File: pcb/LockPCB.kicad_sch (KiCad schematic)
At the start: 0 parts

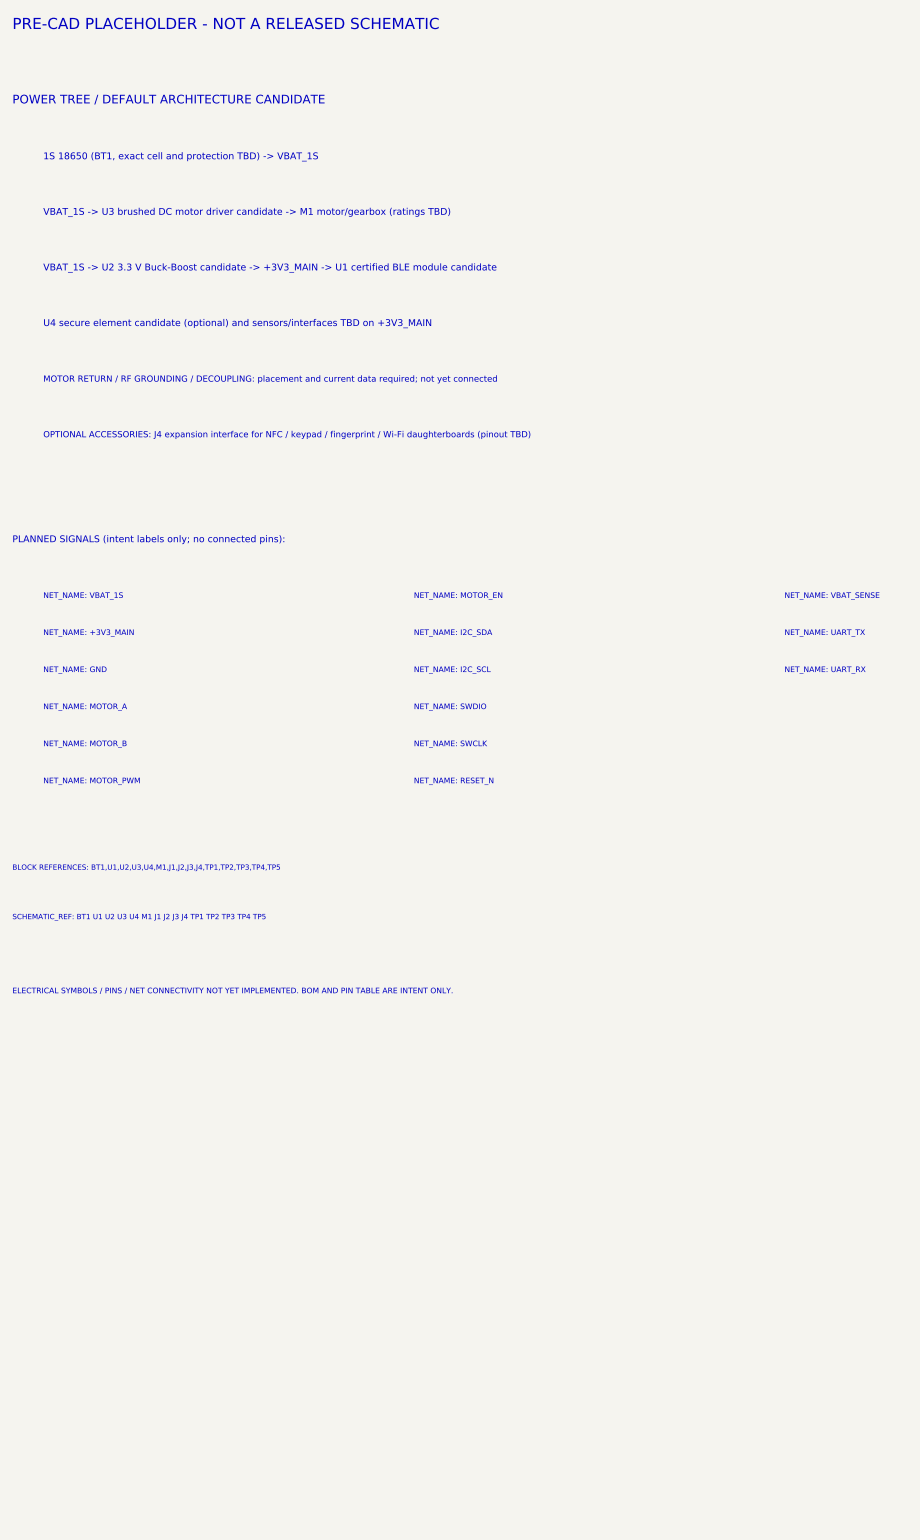
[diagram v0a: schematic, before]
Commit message: Record recommended blocker defaults and review envelope
Co-authored-by: arena-agent <297053741+arena-agent@users.noreply.github.com>
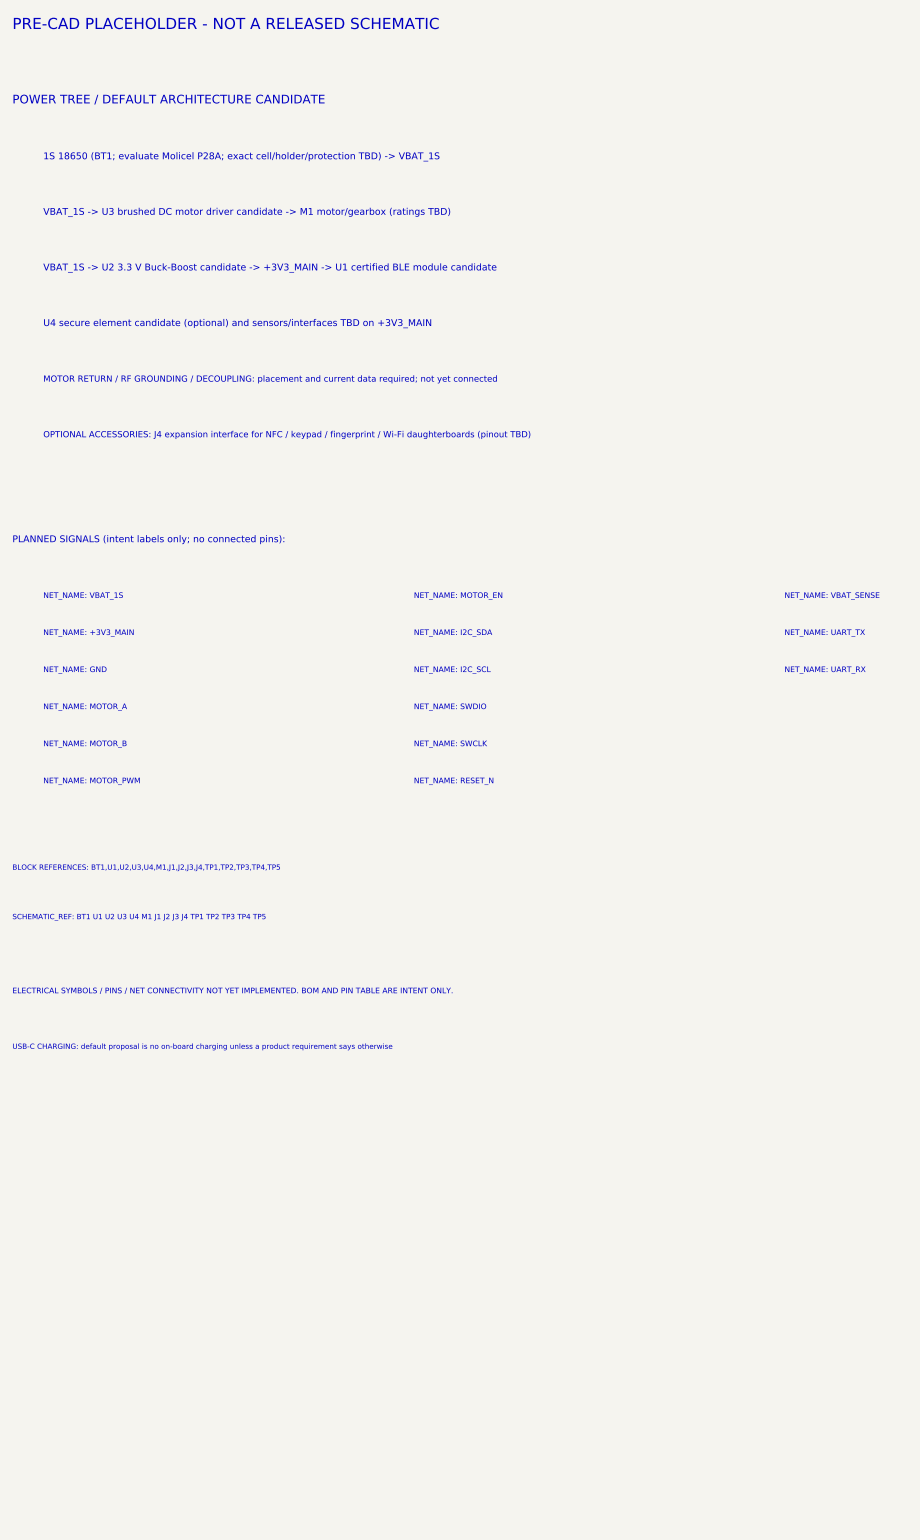
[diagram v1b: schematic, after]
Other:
- note added: "1S 18650 (BT1; evaluate Molicel P28A; exact cell/holder/protection TBD) -> VBAT_1S"
- note added: "USB-C CHARGING: default proposal is no on-board charging unless a product requirement says otherwise"
- note removed: "1S 18650 (BT1, exact cell and protection TBD) -> VBAT_1S"
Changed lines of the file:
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@@
   (text "PRE-CAD PLACEHOLDER - NOT A RELEASED SCHEMATIC" (at 25 28 0) (effects (font (size 1.8 1.8)) (justify left bottom)))
   (text "POWER TREE / DEFAULT ARCHITECTURE CANDIDATE" (at 25 40 0) (effects (font (size 1.4 1.4)) (justify left bottom)))
-  (text "1S 18650 (BT1, exact cell and protection TBD) -> VBAT_1S" (at 30 49 0) (effects (font (size 1.1 1.1)) (justify left bottom)))
+  (text "1S 18650 (BT1; evaluate Molicel P28A; exact cell/holder/protection TBD) -> VBAT_1S" (at 30 49 0) (effects (font (size 1.1 1.1)) (justify left bottom)))
   (text "VBAT_1S -> U3 brushed DC motor driver candidate -> M1 motor/gearbox (ratings TBD)" (at 30 58 0) (effects (font (size 1.1 1.1)) (justify left bottom)))
   (text "VBAT_1S -> U2 3.3 V Buck-Boost candidate -> +3V3_MAIN -> U1 certified BLE module candidate" (at 30 67 0) (effects (font (size 1.1 1.1)) (justify left bottom)))
@@
   (text "SCHEMATIC_REF: BT1 U1 U2 U3 U4 M1 J1 J2 J3 J4 TP1 TP2 TP3 TP4 TP5" (at 25 172 0) (effects (font (size 0.85 0.85)) (justify left bottom)))
   (text "ELECTRICAL SYMBOLS / PINS / NET CONNECTIVITY NOT YET IMPLEMENTED. BOM AND PIN TABLE ARE INTENT ONLY." (at 25 184 0) (effects (font (size 0.9 0.9)) (justify left bottom)))
+  (text "USB-C CHARGING: default proposal is no on-board charging unless a product requirement says otherwise" (at 25 193 0) (effects (font (size 0.85 0.85)) (justify left bottom)))
   (sheet_instances (path "/" (page "1")))
 )

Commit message: Reconcile Drive CAD history and expand interface intent
Co-authored-by: arena-agent <297053741+arena-agent@users.noreply.github.com>
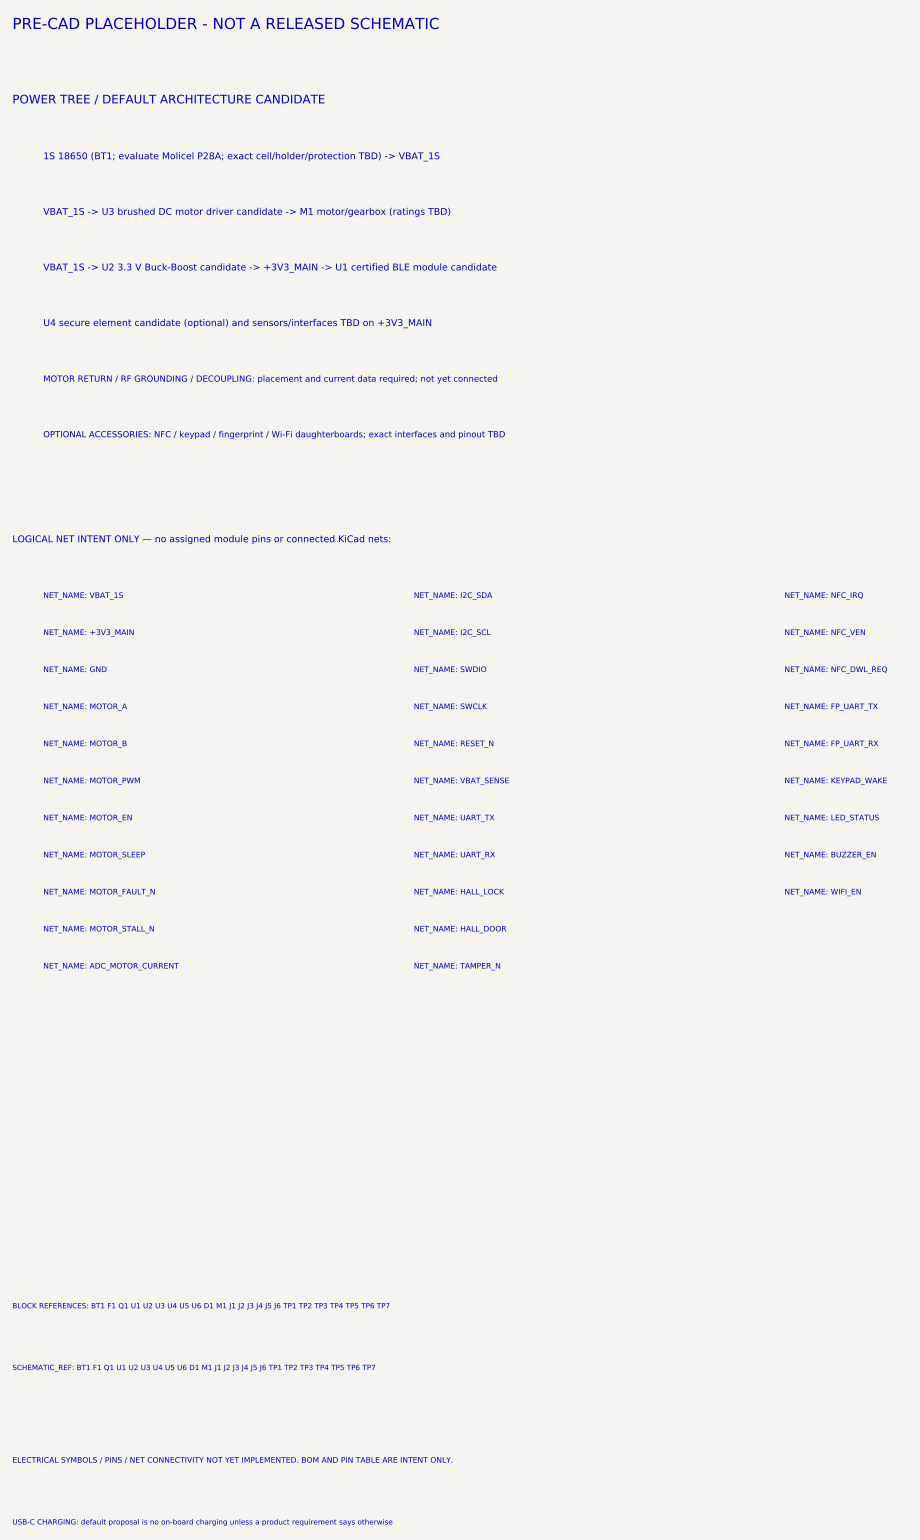
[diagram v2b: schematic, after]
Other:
- note added: "BLOCK REFERENCES: BT1 F1 Q1 U1 U2 U3 U4 U5 U6 D1 M1 J1 J2 J3 J4 J5 J6 TP1 TP2 TP3 TP4 TP5 TP6 TP7"
- note added: "LOGICAL NET INTENT ONLY — no assigned module pins or connected KiCad nets:"
- note added: "NET_NAME: ADC_MOTOR_CURRENT"
- note added: "NET_NAME: BUZZER_EN"
- note added: "NET_NAME: FP_UART_RX"
- note added: "NET_NAME: FP_UART_TX"
- note added: "NET_NAME: HALL_DOOR"
- note added: "NET_NAME: HALL_LOCK"
- note added: "NET_NAME: KEYPAD_WAKE"
- note added: "NET_NAME: LED_STATUS"
- note added: "NET_NAME: MOTOR_FAULT_N"
- note added: "NET_NAME: MOTOR_SLEEP"
- note added: "NET_NAME: MOTOR_STALL_N"
- note added: "NET_NAME: NFC_DWL_REQ"
- note added: "NET_NAME: NFC_IRQ"
- note added: "NET_NAME: NFC_VEN"
- note added: "NET_NAME: TAMPER_N"
- note added: "NET_NAME: WIFI_EN"
- note added: "OPTIONAL ACCESSORIES: NFC / keypad / fingerprint / Wi-Fi daughterboards; exact interfaces and pinout TBD"
- note added: "SCHEMATIC_REF: BT1 F1 Q1 U1 U2 U3 U4 U5 U6 D1 M1 J1 J2 J3 J4 J5 J6 TP1 TP2 TP3 TP4 TP5 TP6 TP7"
- note removed: "BLOCK REFERENCES: BT1,U1,U2,U3,U4,M1,J1,J2,J3,J4,TP1,TP2,TP3,TP4,TP5"
- note removed: "OPTIONAL ACCESSORIES: J4 expansion interface for NFC / keypad / fingerprint / Wi-Fi daughterboards (pinout TBD)"
- note removed: "PLANNED SIGNALS (intent labels only; no connected pins):"
- note removed: "SCHEMATIC_REF: BT1 U1 U2 U3 U4 M1 J1 J2 J3 J4 TP1 TP2 TP3 TP4 TP5"
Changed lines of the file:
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@@
 (kicad_sch (version 20231120) (generator "eeschema")
-  (paper "A4")
+  (paper "A3")
   (title_block
     (title "Matchbox Smart Lock - Electrical Architecture Draft")
@@
   (text "U4 secure element candidate (optional) and sensors/interfaces TBD on +3V3_MAIN" (at 30 76 0) (effects (font (size 1.1 1.1)) (justify left bottom)))
   (text "MOTOR RETURN / RF GROUNDING / DECOUPLING: placement and current data required; not yet connected" (at 30 85 0) (effects (font (size 1.0 1.0)) (justify left bottom)))
-  (text "OPTIONAL ACCESSORIES: J4 expansion interface for NFC / keypad / fingerprint / Wi-Fi daughterboards (pinout TBD)" (at 30 94 0) (effects (font (size 1.0 1.0)) (justify left bottom)))
-  (text "PLANNED SIGNALS (intent labels only; no connected pins):" (at 25 111 0) (effects (font (size 1.1 1.1)) (justify left bottom)))
+  (text "OPTIONAL ACCESSORIES: NFC / keypad / fingerprint / Wi-Fi daughterboards; exact interfaces and pinout TBD" (at 30 94 0) (effects (font (size 1.0 1.0)) (justify left bottom)))
+  (text "LOGICAL NET INTENT ONLY — no assigned module pins or connected KiCad nets:" (at 25 111 0) (effects (font (size 1.1 1.1)) (justify left bottom)))
   (text "NET_NAME: VBAT_1S" (at 30 120 0) (effects (font (size 0.9 0.9)) (justify left bottom)))
   (text "NET_NAME: +3V3_MAIN" (at 30 126 0) (effects (font (size 0.9 0.9)) (justify left bottom)))
@@
   (text "NET_NAME: MOTOR_B" (at 30 144 0) (effects (font (size 0.9 0.9)) (justify left bottom)))
   (text "NET_NAME: MOTOR_PWM" (at 30 150 0) (effects (font (size 0.9 0.9)) (justify left bottom)))
-  (text "NET_NAME: MOTOR_EN" (at 90 120 0) (effects (font (size 0.9 0.9)) (justify left bottom)))
-  (text "NET_NAME: I2C_SDA" (at 90 126 0) (effects (font (size 0.9 0.9)) (justify left bottom)))
-  (text "NET_NAME: I2C_SCL" (at 90 132 0) (effects (font (size 0.9 0.9)) (justify left bottom)))
-  (text "NET_NAME: SWDIO" (at 90 138 0) (effects (font (size 0.9 0.9)) (justify left bottom)))
-  (text "NET_NAME: SWCLK" (at 90 144 0) (effects (font (size 0.9 0.9)) (justify left bottom)))
-  (text "NET_NAME: RESET_N" (at 90 150 0) (effects (font (size 0.9 0.9)) (justify left bottom)))
-  (text "NET_NAME: VBAT_SENSE" (at 150 120 0) (effects (font (size 0.9 0.9)) (justify left bottom)))
-  (text "NET_NAME: UART_TX" (at 150 126 0) (effects (font (size 0.9 0.9)) (justify left bottom)))
-  (text "NET_NAME: UART_RX" (at 150 132 0) (effects (font (size 0.9 0.9)) (justify left bottom)))
-  (text "BLOCK REFERENCES: BT1,U1,U2,U3,U4,M1,J1,J2,J3,J4,TP1,TP2,TP3,TP4,TP5" (at 25 164 0) (effects (font (size 0.85 0.85)) (justify left bottom)))
-  (text "SCHEMATIC_REF: BT1 U1 U2 U3 U4 M1 J1 J2 J3 J4 TP1 TP2 TP3 TP4 TP5" (at 25 172 0) (effects (font (size 0.85 0.85)) (justify left bottom)))
-  (text "ELECTRICAL SYMBOLS / PINS / NET CONNECTIVITY NOT YET IMPLEMENTED. BOM AND PIN TABLE ARE INTENT ONLY." (at 25 184 0) (effects (font (size 0.9 0.9)) (justify left bottom)))
-  (text "USB-C CHARGING: default proposal is no on-board charging unless a product requirement says otherwise" (at 25 193 0) (effects (font (size 0.85 0.85)) (justify left bottom)))
+  (text "NET_NAME: MOTOR_EN" (at 30 156 0) (effects (font (size 0.9 0.9)) (justify left bottom)))
+  (text "NET_NAME: MOTOR_SLEEP" (at 30 162 0) (effects (font (size 0.9 0.9)) (justify left bottom)))
+  (text "NET_NAME: MOTOR_FAULT_N" (at 30 168 0) (effects (font (size 0.9 0.9)) (justify left bottom)))
+  (text "NET_NAME: MOTOR_STALL_N" (at 30 174 0) (effects (font (size 0.9 0.9)) (justify left bottom)))
+  (text "NET_NAME: ADC_MOTOR_CURRENT" (at 30 180 0) (effects (font (size 0.9 0.9)) (justify left bottom)))
+  (text "NET_NAME: I2C_SDA" (at 90 120 0) (effects (font (size 0.9 0.9)) (justify left bottom)))
+  (text "NET_NAME: I2C_SCL" (at 90 126 0) (effects (font (size 0.9 0.9)) (justify left bottom)))
+  (text "NET_NAME: SWDIO" (at 90 132 0) (effects (font (size 0.9 0.9)) (justify left bottom)))
+  (text "NET_NAME: SWCLK" (at 90 138 0) (effects (font (size 0.9 0.9)) (justify left bottom)))
+  (text "NET_NAME: RESET_N" (at 90 144 0) (effects (font (size 0.9 0.9)) (justify left bottom)))
+  (text "NET_NAME: VBAT_SENSE" (at 90 150 0) (effects (font (size 0.9 0.9)) (justify left bottom)))
+  (text "NET_NAME: UART_TX" (at 90 156 0) (effects (font (size 0.9 0.9)) (justify left bottom)))
+  (text "NET_NAME: UART_RX" (at 90 162 0) (effects (font (size 0.9 0.9)) (justify left bottom)))
+  (text "NET_NAME: HALL_LOCK" (at 90 168 0) (effects (font (size 0.9 0.9)) (justify left bottom)))
+  (text "NET_NAME: HALL_DOOR" (at 90 174 0) (effects (font (size 0.9 0.9)) (justify left bottom)))
+  (text "NET_NAME: TAMPER_N" (at 90 180 0) (effects (font (size 0.9 0.9)) (justify left bottom)))
+  (text "NET_NAME: NFC_IRQ" (at 150 120 0) (effects (font (size 0.9 0.9)) (justify left bottom)))
+  (text "NET_NAME: NFC_VEN" (at 150 126 0) (effects (font (size 0.9 0.9)) (justify left bottom)))
+  (text "NET_NAME: NFC_DWL_REQ" (at 150 132 0) (effects (font (size 0.9 0.9)) (justify left bottom)))
+  (text "NET_NAME: FP_UART_TX" (at 150 138 0) (effects (font (size 0.9 0.9)) (justify left bottom)))
+  (text "NET_NAME: FP_UART_RX" (at 150 144 0) (effects (font (size 0.9 0.9)) (justify left bottom)))
+  (text "NET_NAME: KEYPAD_WAKE" (at 150 150 0) (effects (font (size 0.9 0.9)) (justify left bottom)))
+  (text "NET_NAME: LED_STATUS" (at 150 156 0) (effects (font (size 0.9 0.9)) (justify left bottom)))
+  (text "NET_NAME: BUZZER_EN" (at 150 162 0) (effects (font (size 0.9 0.9)) (justify left bottom)))
+  (text "NET_NAME: WIFI_EN" (at 150 168 0) (effects (font (size 0.9 0.9)) (justify left bottom)))
+  (text "BLOCK REFERENCES: BT1 F1 Q1 U1 U2 U3 U4 U5 U6 D1 M1 J1 J2 J3 J4 J5 J6 TP1 TP2 TP3 TP4 TP5 TP6 TP7" (at 25 235 0) (effects (font (size 0.85 0.85)) (justify left bottom)))
+  (text "SCHEMATIC_REF: BT1 F1 Q1 U1 U2 U3 U4 U5 U6 D1 M1 J1 J2 J3 J4 J5 J6 TP1 TP2 TP3 TP4 TP5 TP6 TP7" (at 25 245 0) (effects (font (size 0.85 0.85)) (justify left bottom)))
+  (text "ELECTRICAL SYMBOLS / PINS / NET CONNECTIVITY NOT YET IMPLEMENTED. BOM AND PIN TABLE ARE INTENT ONLY." (at 25 260 0) (effects (font (size 0.9 0.9)) (justify left bottom)))
+  (text "USB-C CHARGING: default proposal is no on-board charging unless a product requirement says otherwise" (at 25 270 0) (effects (font (size 0.85 0.85)) (justify left bottom)))
   (sheet_instances (path "/" (page "1")))
 )

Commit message: Reset CAD handoff to confirmed mechanical baseline
Co-authored-by: arena-agent <297053741+arena-agent@users.noreply.github.com>
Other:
- note added: "1S cell (BT1; 18500 vs 18650 unresolved; cell/holder/protection TBD) -> VBAT_1S"
- note removed: "1S 18650 (BT1; evaluate Molicel P28A; exact cell/holder/protection TBD) -> VBAT_1S"
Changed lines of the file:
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@@
   (text "PRE-CAD PLACEHOLDER - NOT A RELEASED SCHEMATIC" (at 25 28 0) (effects (font (size 1.8 1.8)) (justify left bottom)))
   (text "POWER TREE / DEFAULT ARCHITECTURE CANDIDATE" (at 25 40 0) (effects (font (size 1.4 1.4)) (justify left bottom)))
-  (text "1S 18650 (BT1; evaluate Molicel P28A; exact cell/holder/protection TBD) -> VBAT_1S" (at 30 49 0) (effects (font (size 1.1 1.1)) (justify left bottom)))
+  (text "1S cell (BT1; 18500 vs 18650 unresolved; cell/holder/protection TBD) -> VBAT_1S" (at 30 49 0) (effects (font (size 1.1 1.1)) (justify left bottom)))
   (text "VBAT_1S -> U3 brushed DC motor driver candidate -> M1 motor/gearbox (ratings TBD)" (at 30 58 0) (effects (font (size 1.1 1.1)) (justify left bottom)))
   (text "VBAT_1S -> U2 3.3 V Buck-Boost candidate -> +3V3_MAIN -> U1 certified BLE module candidate" (at 30 67 0) (effects (font (size 1.1 1.1)) (justify left bottom)))

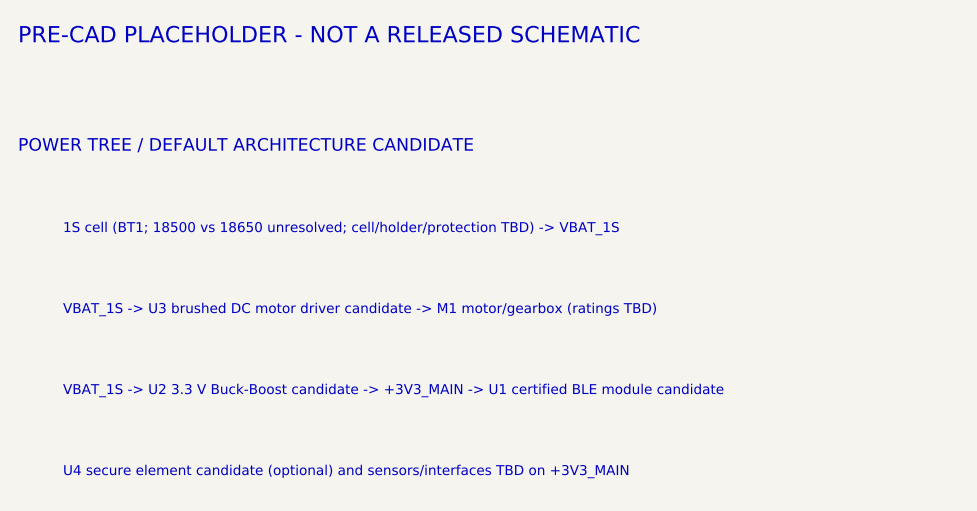
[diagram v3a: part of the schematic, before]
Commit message: Set V1 PCB target to 18650 variant
Co-authored-by: arena-agent <297053741+arena-agent@users.noreply.github.com>
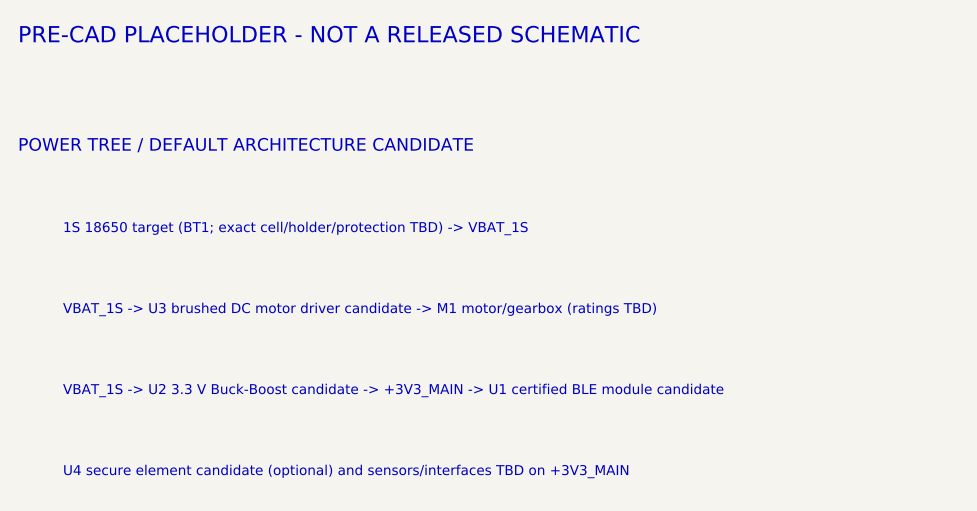
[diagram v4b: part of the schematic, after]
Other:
- note added: "1S 18650 target (BT1; exact cell/holder/protection TBD) -> VBAT_1S"
- note removed: "1S cell (BT1; 18500 vs 18650 unresolved; cell/holder/protection TBD) -> VBAT_1S"
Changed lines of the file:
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@@
   (text "PRE-CAD PLACEHOLDER - NOT A RELEASED SCHEMATIC" (at 25 28 0) (effects (font (size 1.8 1.8)) (justify left bottom)))
   (text "POWER TREE / DEFAULT ARCHITECTURE CANDIDATE" (at 25 40 0) (effects (font (size 1.4 1.4)) (justify left bottom)))
-  (text "1S cell (BT1; 18500 vs 18650 unresolved; cell/holder/protection TBD) -> VBAT_1S" (at 30 49 0) (effects (font (size 1.1 1.1)) (justify left bottom)))
+  (text "1S 18650 target (BT1; exact cell/holder/protection TBD) -> VBAT_1S" (at 30 49 0) (effects (font (size 1.1 1.1)) (justify left bottom)))
   (text "VBAT_1S -> U3 brushed DC motor driver candidate -> M1 motor/gearbox (ratings TBD)" (at 30 58 0) (effects (font (size 1.1 1.1)) (justify left bottom)))
   (text "VBAT_1S -> U2 3.3 V Buck-Boost candidate -> +3V3_MAIN -> U1 certified BLE module candidate" (at 30 67 0) (effects (font (size 1.1 1.1)) (justify left bottom)))
